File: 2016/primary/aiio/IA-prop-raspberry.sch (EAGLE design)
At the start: 73 parts, among them U1 ARDUINO_R3_SHIELD

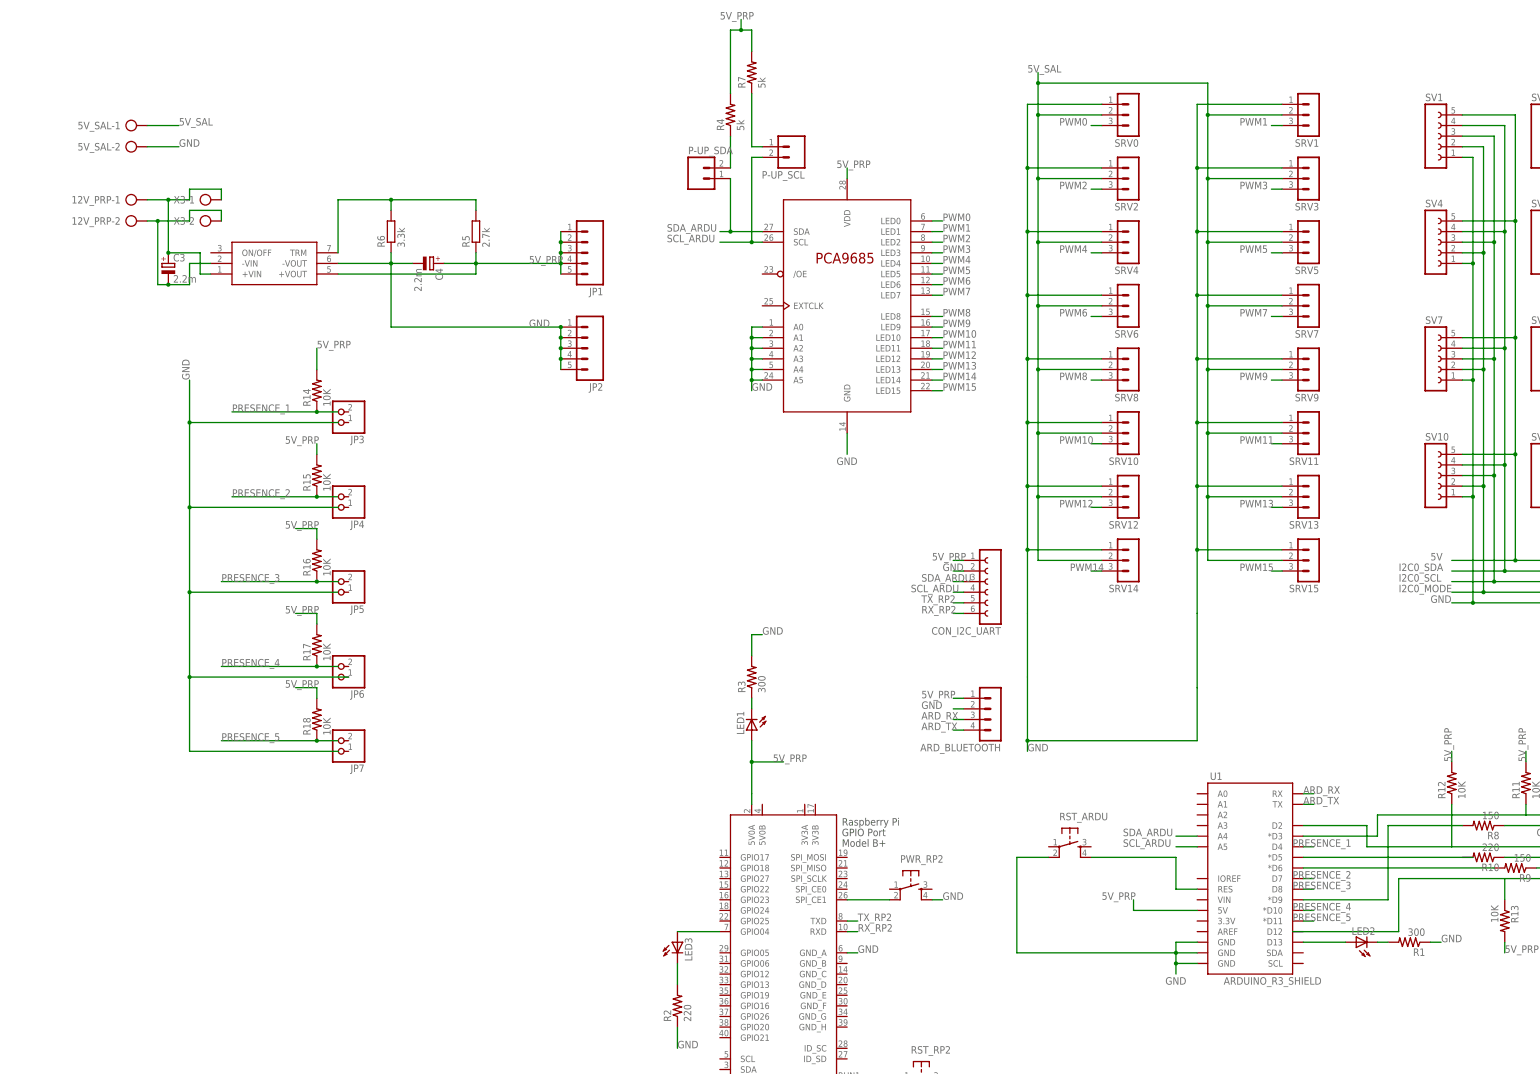
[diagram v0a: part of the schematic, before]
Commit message: [AIIO boards] Put files in directories wrt the year.
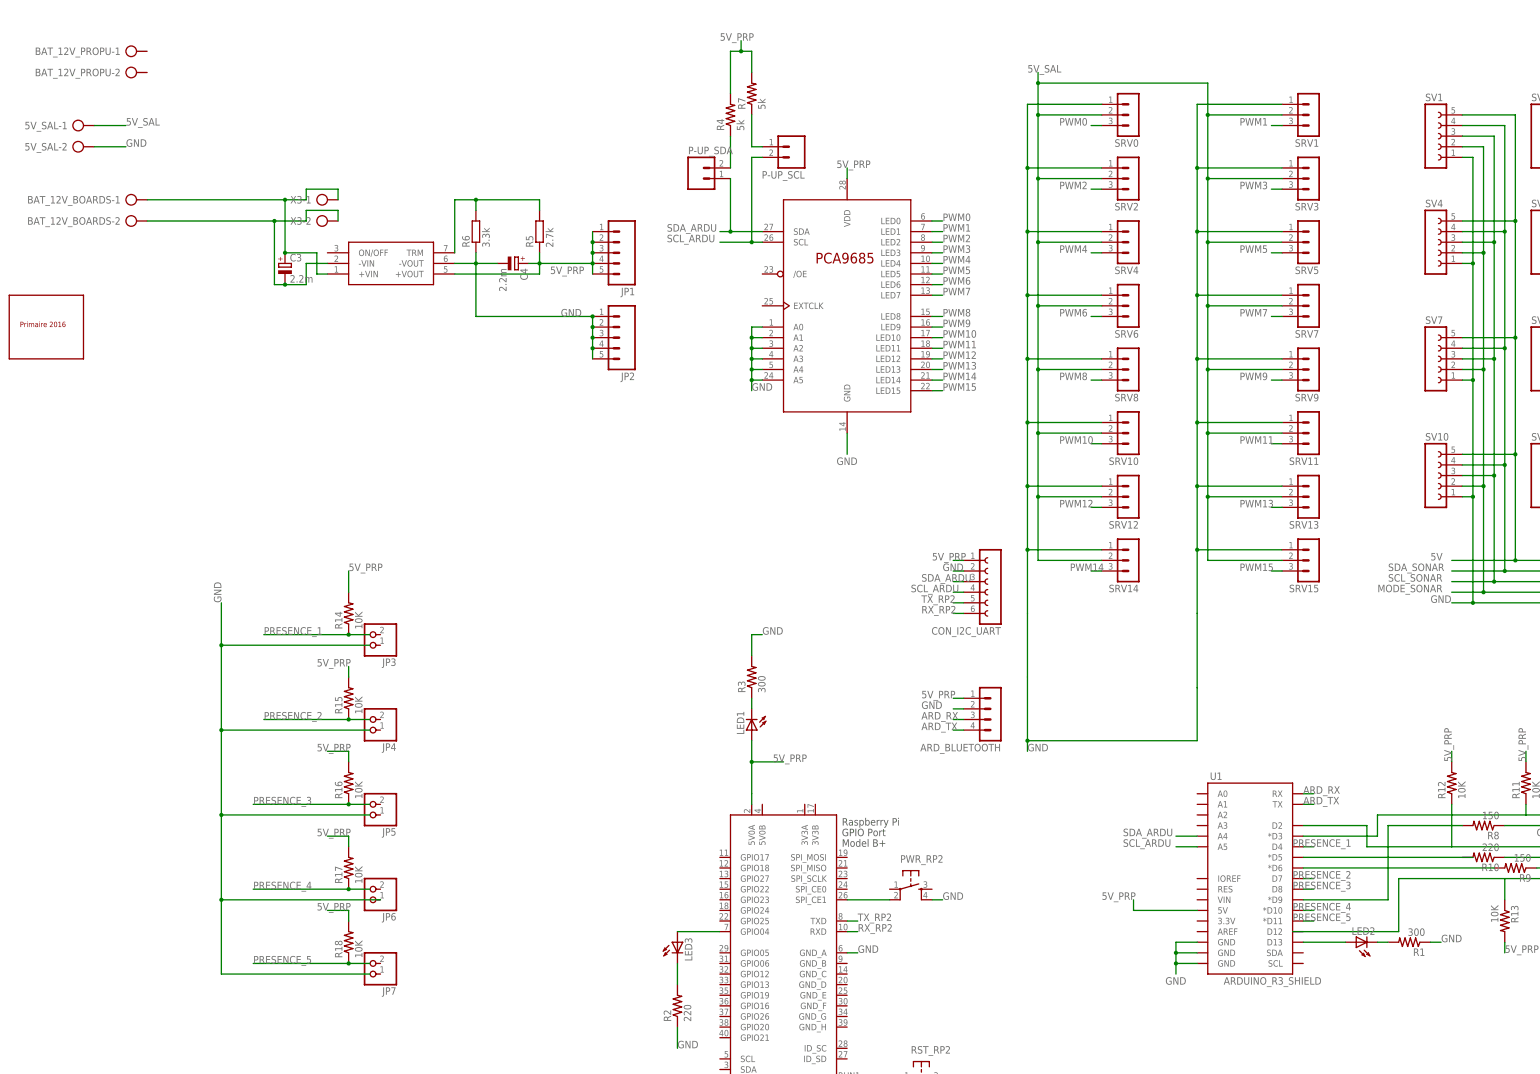
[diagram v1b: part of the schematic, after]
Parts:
- removed RST_ARDU: (no value), SparkFun:TAC_SWITCHPTH
- added BAT_12V_PROPU: (no value), con-ptr500:AK300/2
- added U$3: FOOTPRINT_PRIMAIRE2016, footprintPrimaire2016:FOOTPRINT_PRIMAIRE2016
- renumbered 12V_PRP to BAT_12V_BOARDS
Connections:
- net I2C0_MODE renamed MODE_SONAR
- net I2C0_SCL renamed SCL_SONAR
- net I2C0_SDA renamed SDA_SONAR
- removed net N$8: RST_ARDU.4, U1.RES
- net GND: no longer RST_ARDU.2
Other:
- moved on the sheet: 5V_SAL-1, 5V_SAL-2, C3, C4, JP1, JP2, JP3, JP4, JP5, JP6, JP7, R14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

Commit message: [AIIO_boards] Create and add components for IHM_BOARD.
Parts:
- added 12V_BOARDS, 12V_BOARDS_SRC, 12V_PROPU_SRC: (no value), con-ptr500:AK300/2
- added BOARDIHM_CON_IHM: (no value), con-lsta:FE06-1
- added LED4, LED5: (no value), adafruit:LED5MM
- added LED6: RGBLED_CA-5MM, adafruit:RGBLED_CA-5MM
- added R19, R20: 680, SparkFun:RESISTORAXIAL-0.3
- added U$10: CORD, club:CORD
- added U$4: BAU, club:BAU
- added U$5: FUSE, club:FUSE
- added U$6, U$8: SWITCH_01, club:SWITCH_01
- added U$7: FUSE_BOARDS, club:FUSE_BOARDS
- added U$9: PUSH_BUT_COL_SELEC, club:PUSH_BUT_COL_SELEC
- BAT_12V_BOARDS: OC_FARNELL (none) -> unknown; OC_NEWARK (none) -> unknown
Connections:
- new net BAT_12V_BOARDS+: BAT_12V_BOARDS-1.KL, U$7.P$1
- new net BAT_12V_BOARDS-: 12V_BOARDS_SRC-2.KL, BAT_12V_BOARDS-2.KL, R20.2
- new net BAT_12V_PROPU+: BAT_12V_PROPU-1.KL, U$4.P$1
- new net BAT_12V_PROPU-: 12V_PROPU_SRC-2.KL, BAT_12V_PROPU-2.KL, R19.2
- new net BOARDIHM_GND: BOARDIHM_CON_IHM.3, LED6.VCC, U$10.P$2
- new net N$10: U$5.P$2, U$6.P$1
- new net N$11: 12V_PROPU_SRC-1.KL, LED4.A, U$6.P$2
- new net N$12: LED4.C, R19.1
- new net N$13: U$7.P$2, U$8.P$1
- new net N$14: 12V_BOARDS_SRC-1.KL, LED5.A, U$8.P$2
- new net N$15: BOARDIHM_CON_IHM.2, LED6.RED
- new net N$16: LED5.C, R20.1
- new net N$18: BOARDIHM_CON_IHM.4, U$10.P$1
- new net N$51: BOARDIHM_CON_IHM.5, LED6.GREEN
- new net N$52: BOARDIHM_CON_IHM.6, LED6.BLUE
- new net N$6: BOARDIHM_CON_IHM.1, U$9.P$1
- new net N$8: U$4.P$2, U$5.P$1
- net +12V: now also 12V_BOARDS-1.KL; no longer BAT_12V_BOARDS-1.KL
- net GND_12: now also 12V_BOARDS-2.KL; no longer BAT_12V_BOARDS-2.KL
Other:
- moved on the sheet: 5V_SAL-1, 5V_SAL-2, BAT_12V_BOARDS-1, BAT_12V_BOARDS-2, BAT_12V_PROPU-1, BAT_12V_PROPU-2

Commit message: [AIIO_boards] Clean schematic and board files.
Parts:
- removed X3: (no value), con-ptr500:AK300/2
- added 12V_BOARDS1, 12V_BOARDS_SRC1, 12V_PROPU_SRC1: (no value), con-ptr500:AK300/2
- added U$11: FOOTPRINT_PRIMAIRE2016, footprintPrimaire2016:FOOTPRINT_PRIMAIRE2016
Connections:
- net +12V: now also 12V_BOARDS1-1.KL; no longer X3-1.KL
- net BAT_12V_BOARDS-: now also 12V_BOARDS_SRC1-2.KL
- net BAT_12V_PROPU-: now also 12V_PROPU_SRC1-2.KL
- net BOARDIHM_GND: now also U$9.P$2
- net GND_12: now also 12V_BOARDS1-2.KL; no longer X3-2.KL
- net N$11: now also 12V_PROPU_SRC1-1.KL
- net N$14: now also 12V_BOARDS_SRC1-1.KL
- net N$39: now also R10.2
- net N$49: now also U1.D12
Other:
- moved on the sheet: ARD_BLUETOOTH, CON_I2C_UART, IHM, JP3, JP4, JP5, JP6, JP7, LED1, LED2, LED3, P-UP_SCL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

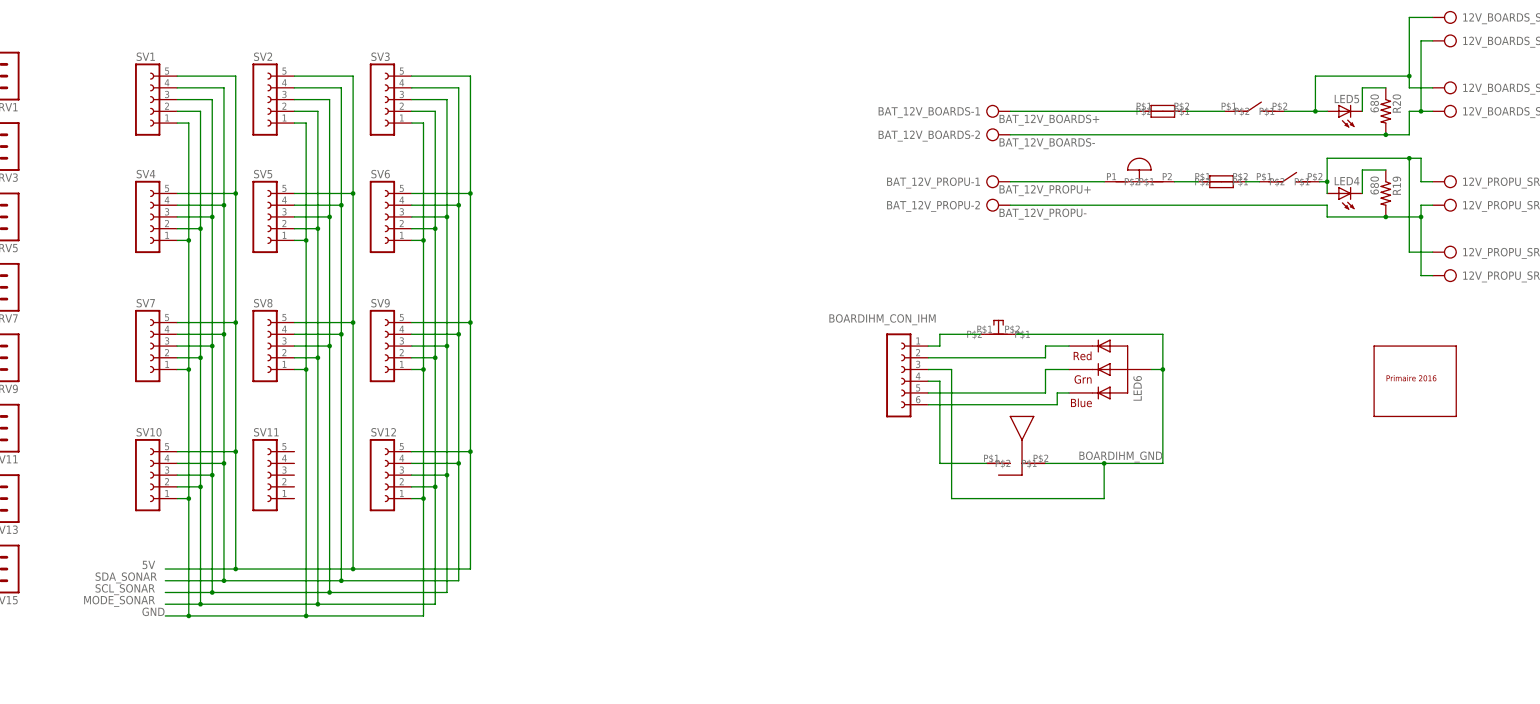
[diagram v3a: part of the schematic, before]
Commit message: [AIIO_board]Place connectors for sonar connectors.
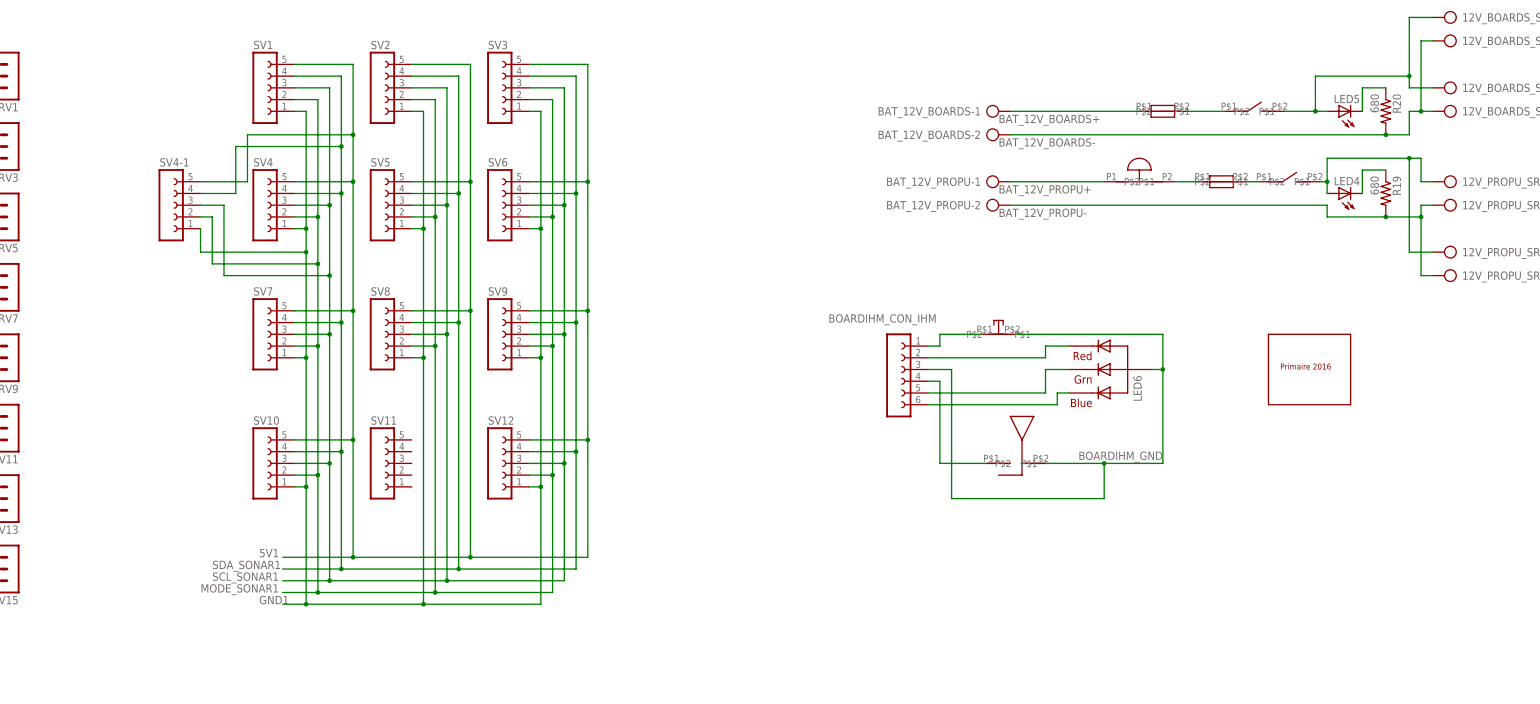
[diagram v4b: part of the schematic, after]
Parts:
- added SV4-1: (no value), con-lsta:FE05-1
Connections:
- removed net 5V: SV1.5, SV10.5, SV12.5, SV2.5, SV3.5, SV4.5, SV5.5, SV6.5, SV7.5, SV8.5, SV9.5
- removed net MODE_SONAR: SV1.2, SV10.2, SV12.2, SV2.2, SV3.2, SV4.2, SV5.2, SV6.2, SV7.2, SV8.2, SV9.2
- removed net SCL_SONAR: SV1.3, SV10.3, SV12.3, SV2.3, SV3.3, SV4.3, SV5.3, SV6.3, SV7.3, SV8.3, SV9.3
- removed net SDA_SONAR: SV1.4, SV10.4, SV12.4, SV2.4, SV3.4, SV4.4, SV5.4, SV6.4, SV7.4, SV8.4, SV9.4
- new net 5V1: SV1.5, SV10.5, SV12.5, SV2.5, SV3.5, SV4-1.5, SV4.5, SV5.5, SV6.5, SV7.5, SV8.5, SV9.5
- new net GND1: SV1.1, SV10.1, SV12.1, SV2.1, SV3.1, SV4-1.1, SV4.1, SV5.1, SV6.1, SV7.1, SV8.1, SV9.1
- new net MODE_SONAR1: SV1.2, SV10.2, SV12.2, SV2.2, SV3.2, SV4-1.2, SV4.2, SV5.2, SV6.2, SV7.2, SV8.2, SV9.2
- new net SCL_SONAR1: SV1.3, SV10.3, SV12.3, SV2.3, SV3.3, SV4-1.3, SV4.3, SV5.3, SV6.3, SV7.3, SV8.3, SV9.3
- new net SDA_SONAR1: SV1.4, SV10.4, SV12.4, SV2.4, SV3.4, SV4-1.4, SV4.4, SV5.4, SV6.4, SV7.4, SV8.4, SV9.4
- net GND: no longer SV1.1, SV10.1, SV12.1, SV2.1, SV3.1, SV4.1, SV5.1, SV6.1, SV7.1, SV8.1, SV9.1
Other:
- moved on the sheet: SV1, SV10, SV11, SV12, SV2, SV3, SV4, SV5, SV6, SV7, SV8, SV9

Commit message: [AIIO_board]Place RP2 and make corrections on I2C_RP2 bus.
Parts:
- removed SV4-1: (no value), con-lsta:FE05-1
- added SV9-1: (no value), con-lsta:FE05-1
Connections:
- removed net 5V1: SV1.5, SV10.5, SV12.5, SV2.5, SV3.5, SV4-1.5, SV4.5, SV5.5, SV6.5, SV7.5, SV8.5, SV9.5
- removed net GND1: SV1.1, SV10.1, SV12.1, SV2.1, SV3.1, SV4-1.1, SV4.1, SV5.1, SV6.1, SV7.1, SV8.1, SV9.1
- removed net MODE_SONAR1: SV1.2, SV10.2, SV12.2, SV2.2, SV3.2, SV4-1.2, SV4.2, SV5.2, SV6.2, SV7.2, SV8.2, SV9.2
- removed net SCL_SONAR1: SV1.3, SV10.3, SV12.3, SV2.3, SV3.3, SV4-1.3, SV4.3, SV5.3, SV6.3, SV7.3, SV8.3, SV9.3
- removed net SDA_SONAR1: SV1.4, SV10.4, SV12.4, SV2.4, SV3.4, SV4-1.4, SV4.4, SV5.4, SV6.4, SV7.4, SV8.4, SV9.4
- new net SCL_RP2: RP2.SCL, SV1.3, SV10.3, SV12.3, SV2.3, SV3.3, SV4.3, SV5.3, SV6.3, SV7.3, SV8.3, SV9-1.3, SV9.3
- new net SDA_RP2: RP2.SDA, SV1.4, SV10.4, SV12.4, SV2.4, SV3.4, SV4.4, SV5.4, SV6.4, SV7.4, SV8.4, SV9-1.4, SV9.4
- net 5V_PRP: now also SV1.5, SV10.5, SV12.5, SV2.5, SV3.5, SV4.5, SV5.5, SV6.5, SV7.5, SV8.5, SV9-1.5, SV9.5
- net GND: now also SV1.1, SV10.1, SV12.1, SV2.1, SV3.1, SV4.1, SV5.1, SV6.1, SV7.1, SV8.1, SV9-1.1, SV9.1
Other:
- moved on the sheet: R2

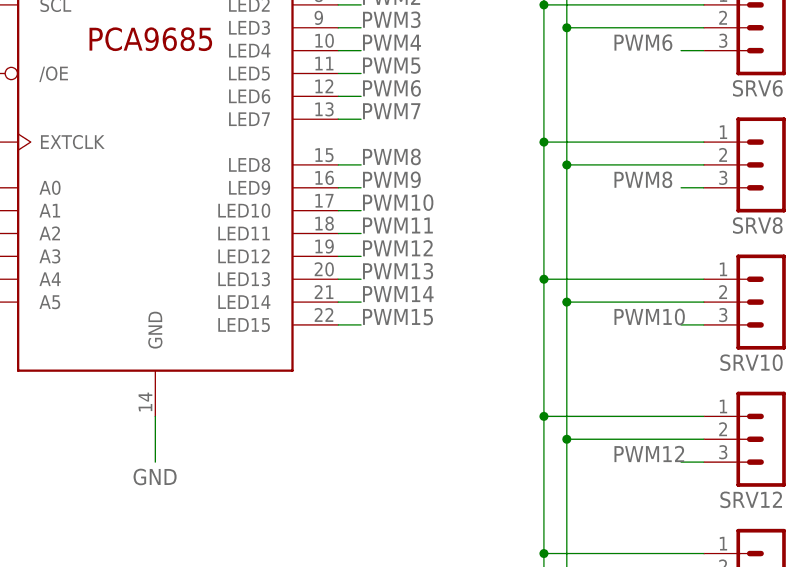
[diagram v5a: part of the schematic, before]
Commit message: [AIIO_boards] Connect servo connectors to PCA9685PW.
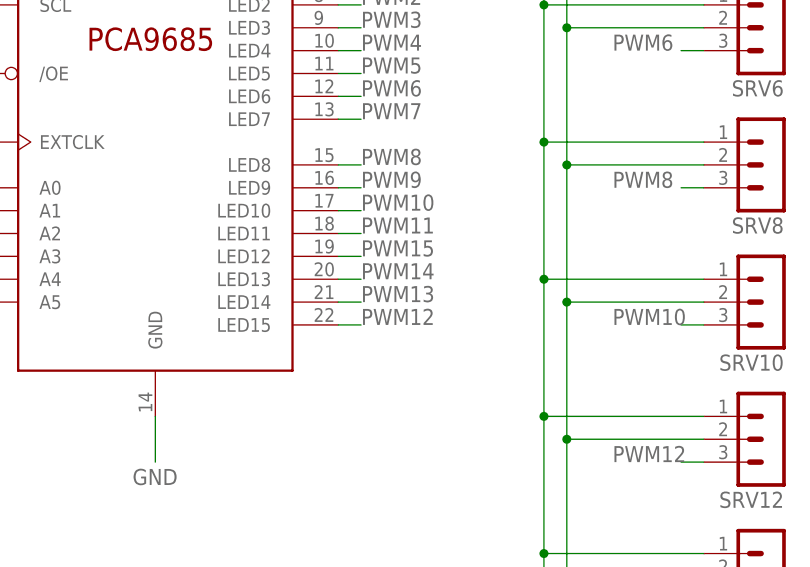
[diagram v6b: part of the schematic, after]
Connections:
- net PWM12: now also U$1.LED15; no longer U$1.LED12
- net PWM13: now also U$1.LED14; no longer U$1.LED13
- net PWM14: now also U$1.LED13; no longer U$1.LED14
- net PWM15: now also U$1.LED12; no longer U$1.LED15
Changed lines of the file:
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@@
 <net name="PWM12" class="0">
+<segment>
+<pinref part="SRV12" gate="G$1" pin="3"/>
+<wire x1="175.26" y1="-30.48" x2="172.72" y2="-30.48" width="0.1524" layer="91"/>
+<label x="165.1" y="-30.48" size="1.778" layer="95"/>
+</segment>
+<segment>
+<pinref part="U$1" gate="G$1" pin="LED15"/>
+<wire x1="134.62" y1="-15.24" x2="137.16" y2="-15.24" width="0.1524" layer="91"/>
+<label x="137.16" y="-15.24" size="1.778" layer="95"/>
+</segment>
+</net>
+<net name="PWM13" class="0">
+<segment>
+<pinref part="SRV13" gate="G$1" pin="3"/>
+<wire x1="218.44" y1="-30.48" x2="215.9" y2="-30.48" width="0.1524" layer="91"/>
+<label x="208.28" y="-30.48" size="1.778" layer="95"/>
+</segment>
+<segment>
+<pinref part="U$1" gate="G$1" pin="LED14"/>
+<wire x1="134.62" y1="-12.7" x2="137.16" y2="-12.7" width="0.1524" layer="91"/>
+<label x="137.16" y="-12.7" size="1.778" layer="95"/>
+</segment>
+</net>
+<net name="PWM14" class="0">
+<segment>
+<pinref part="SRV14" gate="G$1" pin="3"/>
+<wire x1="175.26" y1="-45.72" x2="172.72" y2="-45.72" width="0.1524" layer="91"/>
+<label x="167.64" y="-45.72" size="1.778" layer="95"/>
+</segment>
+<segment>
+<pinref part="U$1" gate="G$1" pin="LED13"/>
+<wire x1="134.62" y1="-10.16" x2="137.16" y2="-10.16" width="0.1524" layer="91"/>
+<label x="137.16" y="-10.16" size="1.778" layer="95"/>
+</segment>
+</net>
+<net name="PWM15" class="0">
+<segment>
+<pinref part="SRV15" gate="G$1" pin="3"/>
+<wire x1="218.44" y1="-45.72" x2="215.9" y2="-45.72" width="0.1524" layer="91"/>
+<label x="208.28" y="-45.72" size="1.778" layer="95"/>
+</segment>
 <segment>
 <pinref part="U$1" gate="G$1" pin="LED12"/>
@@
 <label x="137.16" y="-7.62" size="1.778" layer="95"/>
 </segment>
-<segment>
-<pinref part="SRV12" gate="G$1" pin="3"/>
-<wire x1="175.26" y1="-30.48" x2="172.72" y2="-30.48" width="0.1524" layer="91"/>
-<label x="165.1" y="-30.48" size="1.778" layer="95"/>
-</segment>
 </net>
-<net name="PWM13" class="0">
-<segment>
-<pinref part="U$1" gate="G$1" pin="LED13"/>
-<wire x1="134.62" y1="-10.16" x2="137.16" y2="-10.16" width="0.1524" layer="91"/>
-<label x="137.16" y="-10.16" size="1.778" layer="95"/>
-</segment>
-<segment>
-<pinref part="SRV13" gate="G$1" pin="3"/>
-<wire x1="218.44" y1="-30.48" x2="215.9" y2="-30.48" width="0.1524" layer="91"/>
-<label x="208.28" y="-30.48" size="1.778" layer="95"/>
-</segment>
-</net>
-<net name="PWM14" class="0">
-<segment>
-<pinref part="U$1" gate="G$1" pin="LED14"/>
-<wire x1="134.62" y1="-12.7" x2="137.16" y2="-12.7" width="0.1524" layer="91"/>
-<label x="137.16" y="-12.7" size="1.778" layer="95"/>
-</segment>
-<segment>
-<pinref part="SRV14" gate="G$1" pin="3"/>
-<wire x1="175.26" y1="-45.72" x2="172.72" y2="-45.72" width="0.1524" layer="91"/>
-<label x="167.64" y="-45.72" size="1.778" layer="95"/>
-</segment>
-</net>
-<net name="PWM15" class="0">
-<segment>
-<pinref part="U$1" gate="G$1" pin="LED15"/>
-<wire x1="134.62" y1="-15.24" x2="137.16" y2="-15.24" width="0.1524" layer="91"/>
-<label x="137.16" y="-15.24" size="1.778" layer="95"/>
-</segment>
-<segment>
-<pinref part="SRV15" gate="G$1" pin="3"/>
-<wire x1="218.44" y1="-45.72" x2="215.9" y2="-45.72" width="0.1524" layer="91"/>
-<label x="208.28" y="-45.72" size="1.778" layer="95"/>
-</segment>
-</net>
